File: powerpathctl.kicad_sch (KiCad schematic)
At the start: 11 parts, among them J10 Conn_01x06_Male, J11 Conn_01x06_Male_BAT_data, J8 Conn_01x03_Male_BAT_PWR_IN_NU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, J9 Conn_01x03_Male_BAT_PWR, Q1 SI7149ADP-T1-GE3, U7 LTC4412ES6

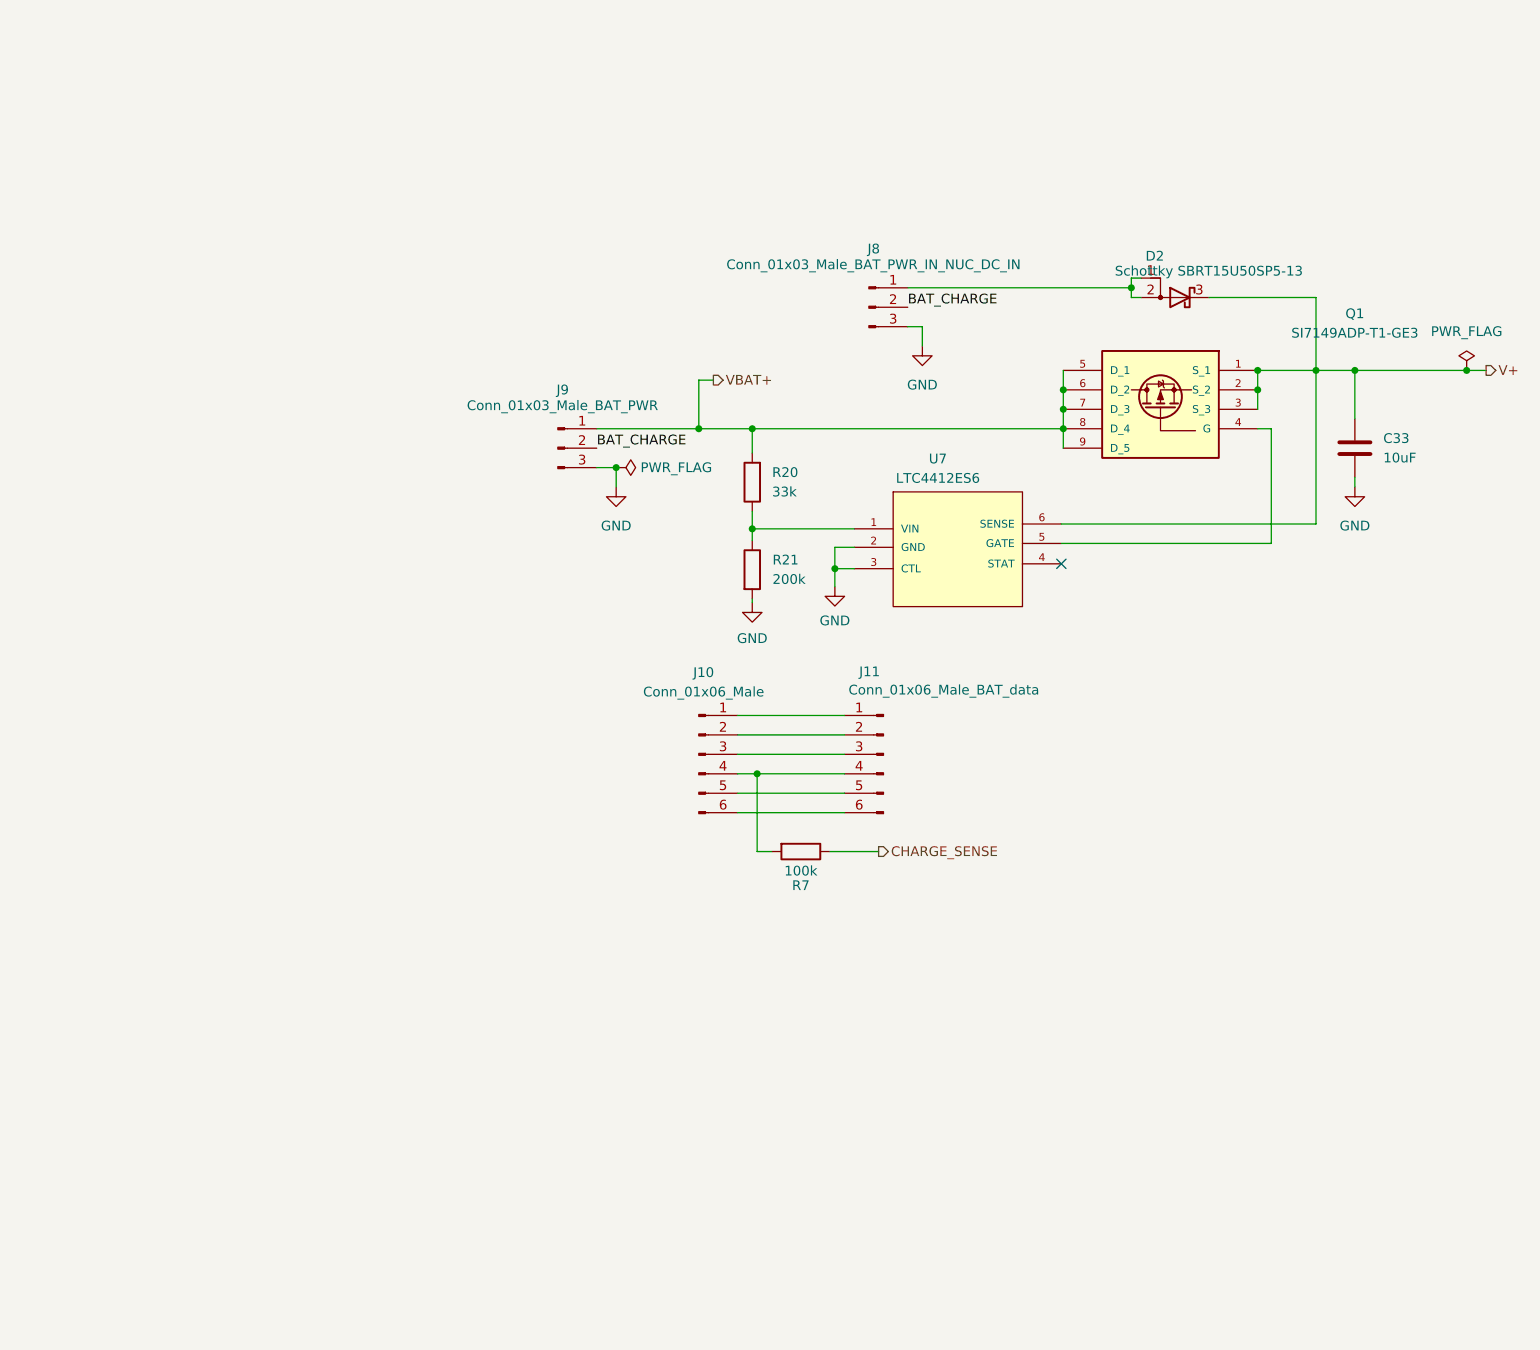
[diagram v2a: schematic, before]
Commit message: Power circuit initial routing
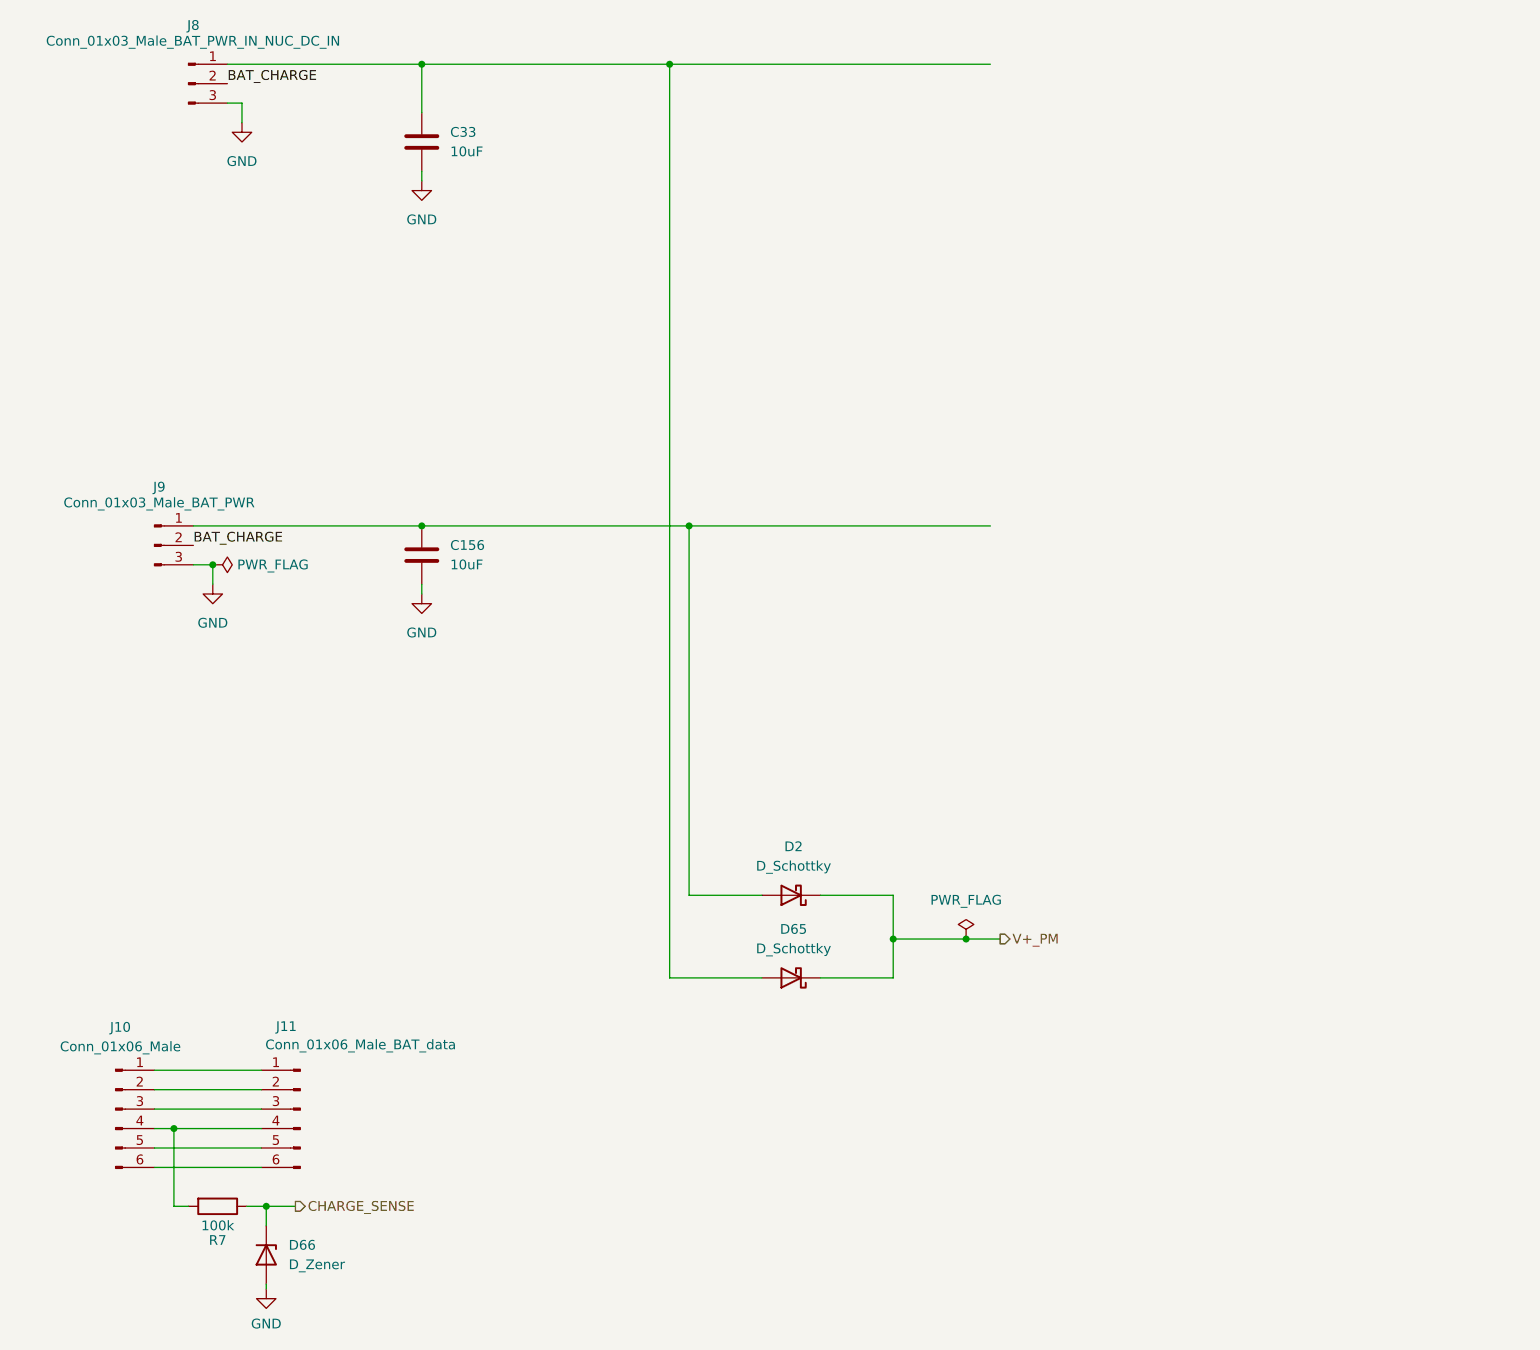
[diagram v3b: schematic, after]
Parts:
- removed D2: Schottky SBRT15U50SP5-13, Diode_SMD:D_PowerDI-5, symbol Device:D_Schottky_AAK
- removed Q1: SI7149ADP-T1-GE3, Robotont:POWERPAKSO-8, symbol SI7149ADP-T1-GE3:SI7149ADP-T1-GE3
- removed R20: 33k, Resistor_SMD:R_0603_1608Metric, symbol Device:R
- removed R21: 200k, Resistor_SMD:R_0603_1608Metric, symbol Device:R
- removed U7: LTC4412ES6, Robotont:TSOT-23_S6, symbol LTC4412ES6:LTC4412ES6
- added C156: 10uF, Capacitor_SMD:C_1206_3216Metric, symbol Device:C
- added D2, D65: D_Schottky, Diode_SMD:D_SMA, symbol Device:D_Schottky
- added D66: D_Zener, Diode_SMD:D_MiniMELF, symbol Device:D_Zener
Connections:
- net V+ is gone; now on an unnamed net: C33.1
- net CHARGE_SENSE: now also D66.1 (K)
- net GND: now also C156.2, D66.2 (A)
- net at J8.1 (Pin_1): now also D65.2 (A)
- net VBAT+: no longer names the net of J9.1 (Pin_1)
- net VBAT+: now also C156.1, D2.2 (A)
- new net V+_PM: D2.1 (K), D65.1 (K)
- no-connect marks 1 -> 0
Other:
- moved on the sheet: C33, J10, J11, J8, J9, R7
